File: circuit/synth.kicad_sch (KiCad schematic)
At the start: 3 parts, among them J1 Raspberry_Pi_4, U1 ADS1115IDGS

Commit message: merge with Kicad file
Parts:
- added R1, R4: 10K, symbol Device:R
- added R2, R3: 1K, symbol Device:R
- added SW_LLM, SW_REC: SW_DIP_x01, symbol Switch:SW_DIP_x01
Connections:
- net at J1.1 (3V3), J1.17 (3V3), RV1.1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: now also R2.2, R3.2
- net at J1.14 (GND), J1.20 (GND), J1.25 (GND)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: now also SW_LLM.1, SW_REC.1
- net at J1.35 (GPIO19/SPI1_MISO/PCM_FS): now also R1.2
- net at J1.37 (GPIO26/SDIO_DAT2): now also R4.2
- new net: R1.1, R2.1, R3.1, SW_REC.2
- new net: R4.1, SW_LLM.2
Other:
- moved on the sheet: RV1, U1

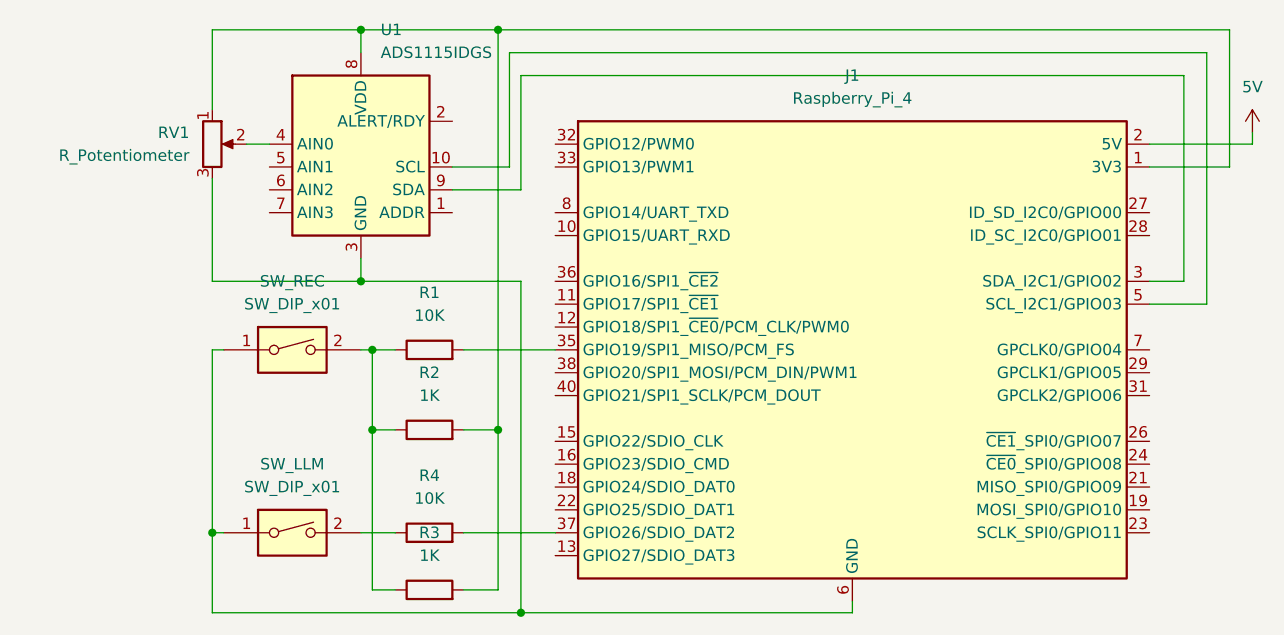
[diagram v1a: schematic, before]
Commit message: modified circuit, wrote README
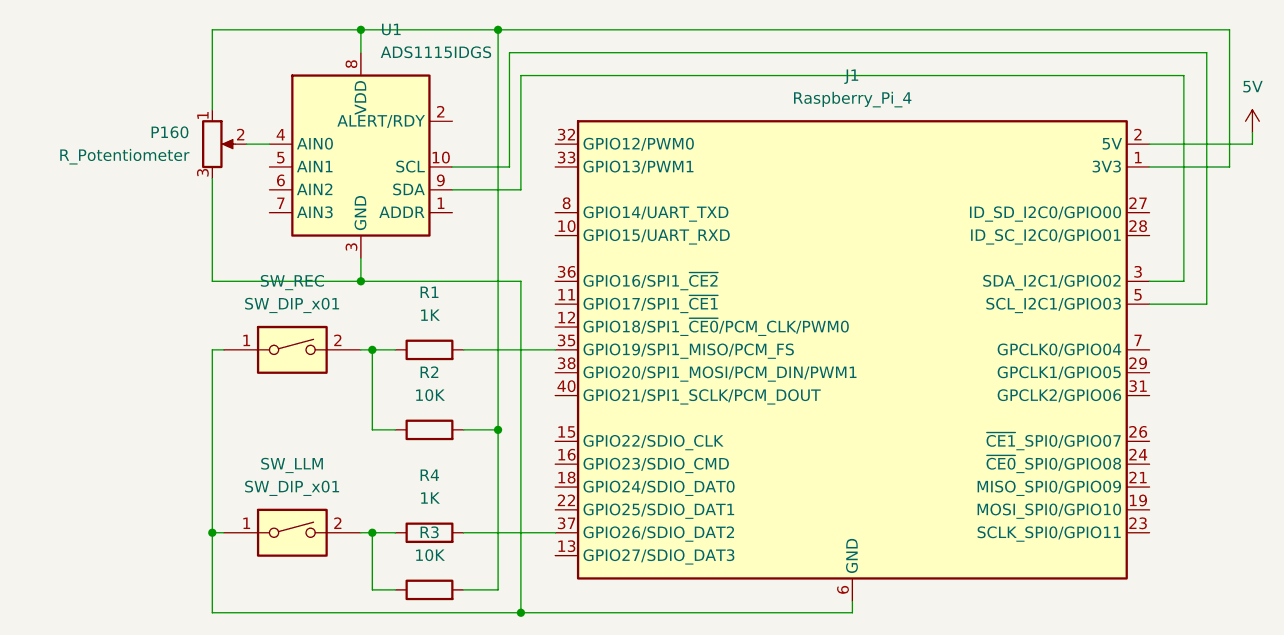
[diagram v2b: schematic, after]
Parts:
- R1, R4: value 10K -> 1K
- R2, R3: value 1K -> 10K
- renumbered RV1 to P160
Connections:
- net at R1.1, R2.1, SW_REC.2: no longer R3.1
- net at R4.1, SW_LLM.2: now also R3.1
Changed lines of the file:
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@@
 	)
 	(junction
-		(at 106.68 85.09)
+		(at 106.68 96.52)
 		(diameter 0)
 		(color 0 0 0 0)
@@
 	(wire
 		(pts
+			(xy 106.68 96.52) (xy 106.68 102.87)
+		)
+		(stroke
+			(width 0)
+			(type default)
+		)
+	)
+	(wire
+		(pts
 			(xy 120.65 40.64) (xy 105.41 40.64)
 		)
@@
 	(wire
 		(pts
+			(xy 106.68 96.52) (xy 109.22 96.52)
+		)
+		(stroke
+			(width 0)
+			(type default)
+		)
+	)
+	(wire
+		(pts
 			(xy 88.9 68.58) (xy 105.41 68.58)
 		)
@@
 	(wire
 		(pts
-			(xy 105.41 96.52) (xy 109.22 96.52)
+			(xy 105.41 96.52) (xy 106.68 96.52)
 		)
 		(stroke
@@
 		(pts
 			(xy 105.41 40.64) (xy 105.41 43.18)
-		)
-		(stroke
-			(width 0)
-			(type default)
-		)
-	)
-	(wire
-		(pts
-			(xy 106.68 102.87) (xy 106.68 85.09)
 		)
 		(stroke
@@
 			)
 		)
-		(property "Value" "1K"
+		(property "Value" "10K"
 			(at 113.03 81.28 90)
 			(effects
@@
 			)
 		)
-		(property "Value" "10K"
+		(property "Value" "1K"
 			(at 113.03 92.71 90)
 			(effects
@@
 		(dnp no)
 		(fields_autoplaced yes)
-		(property "Reference" "RV1"
+		(property "Reference" "P160"
 			(at 86.36 52.0699 0)
 			(effects
@@
 			(project ""
 				(path "/b16a36d3-5bce-4c07-824a-9226f727ef4c"
-					(reference "RV1")
+					(reference "P160")
 					(unit 1)
 				)
@@
 			)
 		)
-		(property "Value" "1K"
+		(property "Value" "10K"
 			(at 113.03 99.06 90)
 			(effects
@@
 			)
 		)
-		(property "Value" "10K"
+		(property "Value" "1K"
 			(at 113.03 72.39 90)
 			(effects
